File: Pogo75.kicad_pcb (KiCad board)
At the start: 2 copper layers, 57 parts, among them J2 Conn_01x05, J3 Conn_01x11, J4 Conn_01x11, J5 Conn_01x11, K1 Mod1, K2 Mod2, K3 Mod3, K4 Mod4, SW1 SW_Push, U1 W25Q128JVS, U3 XC6206PxxxMR-Regulator_Linear, Y1 Crystal_GND24_Small

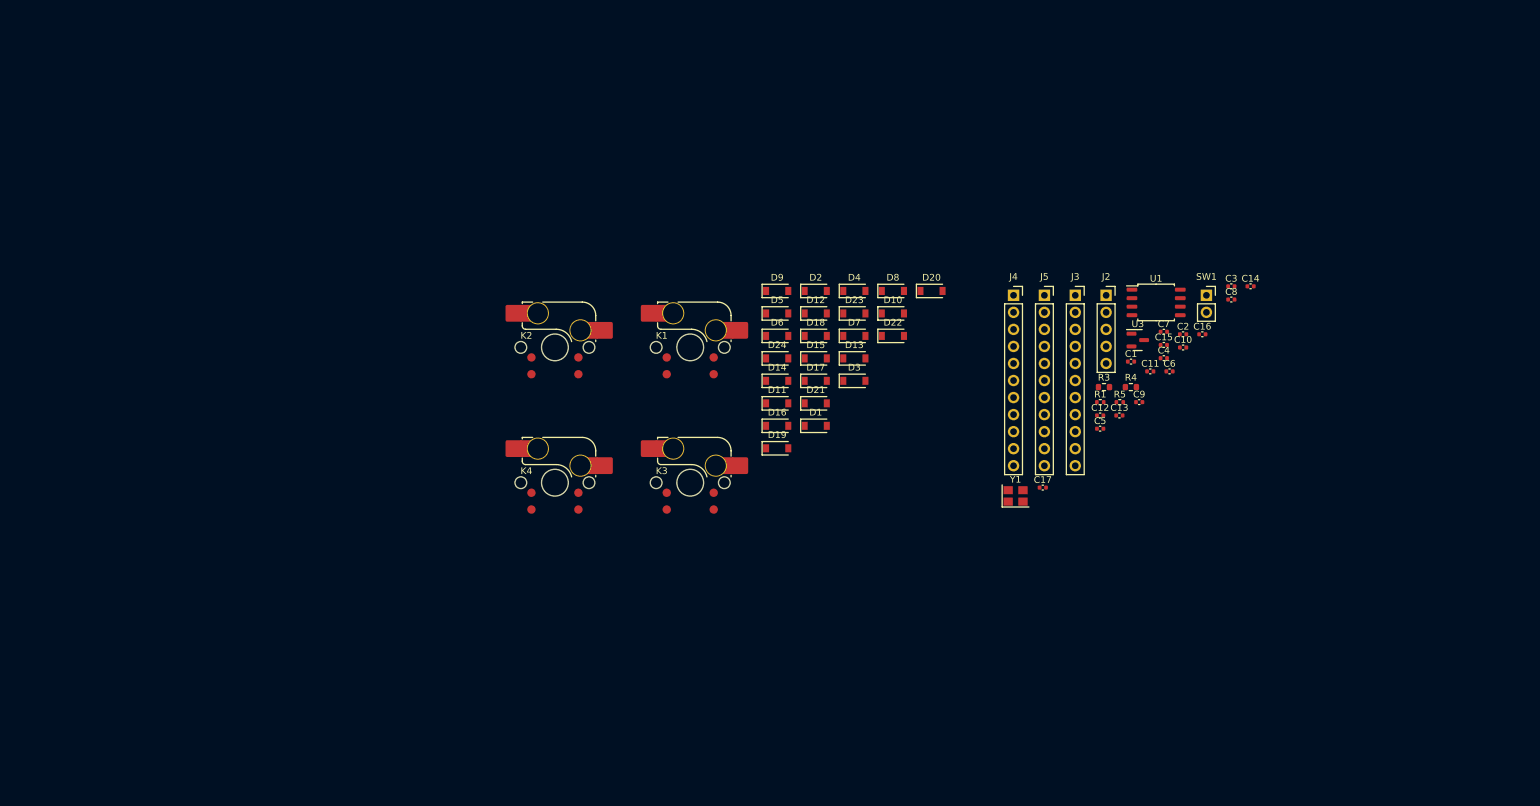
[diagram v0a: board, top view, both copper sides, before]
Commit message: Assigned footprints
Macropad + RP2040
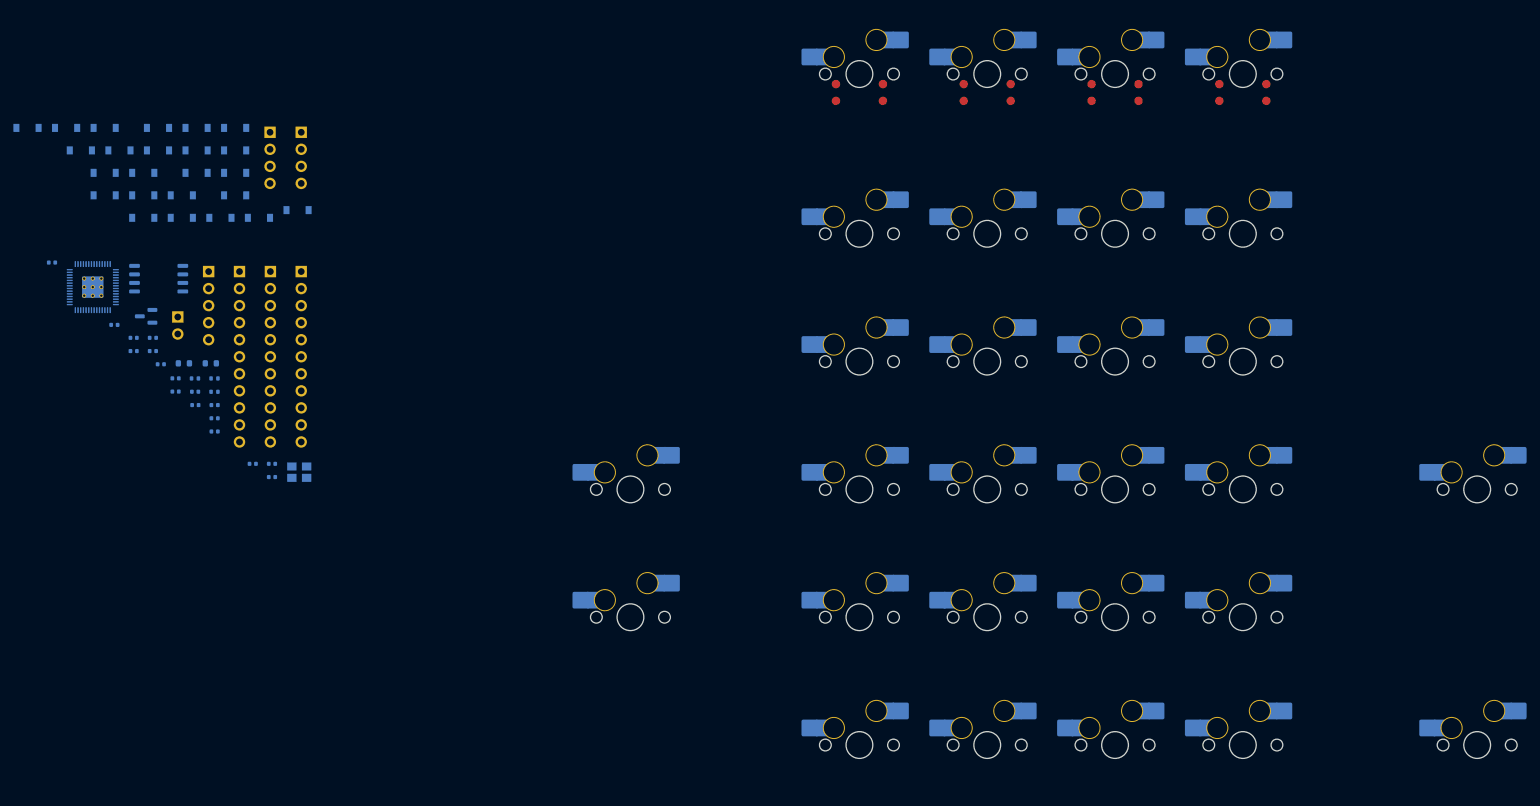
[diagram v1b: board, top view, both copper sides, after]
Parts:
- added F1: OLED1, Connector_PinHeader_2.54mm:PinHeader_1x04_P2.54mm_Vertical, B.Cu at (70.1, 49.2)
- added F2: OLED2, Connector_PinHeader_2.54mm:PinHeader_1x04_P2.54mm_Vertical, B.Cu at (74.8, 49.2)
- added K10: 8, marbastlib-mx:SW_MX_HS_1u, B.Cu at (177.0, 83.3)
- added K11: 9, marbastlib-mx:SW_MX_HS_1u, B.Cu at (196.1, 83.3)
- added K12: SW_Push, marbastlib-mx:SW_MX_HS_1u, B.Cu at (215.1, 83.3)
- added K13: 4, marbastlib-mx:SW_MX_HS_1u, B.Cu at (158.0, 102.4)
- added K14: 5, marbastlib-mx:SW_MX_HS_1u, B.Cu at (177.0, 102.4)
- added K15: 6, marbastlib-mx:SW_MX_HS_1u, B.Cu at (196.1, 102.4)
- added K16: SW_Push, marbastlib-mx:SW_MX_HS_1u, B.Cu at (215.1, 102.4)
- added K17: 1, marbastlib-mx:SW_MX_HS_1u, B.Cu at (158.0, 121.4)
- added K18: 2, marbastlib-mx:SW_MX_HS_1u, B.Cu at (177.0, 121.4)
- added K19: 3, marbastlib-mx:SW_MX_HS_1u, B.Cu at (196.1, 121.4)
- added K20: SW_Push, marbastlib-mx:SW_MX_HS_1u, B.Cu at (215.1, 121.4)
- added K21: 0, marbastlib-mx:SW_MX_HS_1u, B.Cu at (158.0, 140.5)
- added K22: ., marbastlib-mx:SW_MX_HS_1u, B.Cu at (177.0, 140.5)
- added K23: SW_Push, marbastlib-mx:SW_MX_HS_1u, B.Cu at (196.1, 140.5)
- added K24: Enter, marbastlib-mx:SW_MX_HS_1u, B.Cu at (215.1, 140.5)
- added K5: Num, marbastlib-mx:SW_MX_HS_1u, B.Cu at (158.0, 64.3)
- added K6: /, marbastlib-mx:SW_MX_HS_1u, B.Cu at (177.0, 64.3)
- added K7: *, marbastlib-mx:SW_MX_HS_1u, B.Cu at (196.1, 64.3)
- added K8: -, marbastlib-mx:SW_MX_HS_1u, B.Cu at (215.1, 64.3)
- added K9: 7, marbastlib-mx:SW_MX_HS_1u, B.Cu at (158.0, 83.3)
- added KO-1: 4, marbastlib-mx:SW_MX_HS_1u, B.Cu at (123.8, 102.4)
- added KO-2: 4, marbastlib-mx:SW_MX_HS_1u, B.Cu at (250.0, 102.4)
- added KO-3: 4, marbastlib-mx:SW_MX_HS_1u, B.Cu at (123.8, 121.4)
- added KO-4: 4, marbastlib-mx:SW_MX_HS_1u, B.Cu at (250.0, 140.5)
- added R2: R_Small, Resistor_SMD:R_0402_1005Metric, B.Cu at (61.8, 85.9)
- added U2: RP2040, Sleep-footprints:RP2040-QFN-56, B.Cu at (43.7, 72.2)
- C1, C10, C11, C12, C13, C14, C15, C16, C17, C2, C3, C4, C5, C6, C7, C8, C9, D1, D10, D11, D12, D13, D14, D15, D16, D17, D18, D19, D2, D20, D21, D22, D23, D24, D3, D4, D5, D6, D7, D8, D9, J2, J3, J4, J5, K1, K2, K3, K4, R1, R3, R4, R5, SW1, U1, U3, Y1: moved to B.Cu
- moved C14 178.7 mm to (37.6, 68.6), turned to 180 degrees
- moved C10 159.3 mm to (46.9, 77.9), turned to 180 degrees
- moved C16 155.3 mm to (53.8, 83.7), turned to 180 degrees
- moved C8 155.2 mm to (59.0, 89.8), turned to 180 degrees
- moved C15 153.6 mm to (49.8, 79.8), turned to 180 degrees
- moved SW1 153.4 mm to (56.4, 76.7), turned to 180 degrees
- moved C3 152.6 mm to (61.8, 89.8), turned to 180 degrees
- moved C4 150.7 mm to (52.6, 81.8), turned to 180 degrees
- moved U1 148.7 mm to (53.5, 71.0), turned to 180 degrees
- moved C6 148.2 mm to (56.0, 87.8), turned to 180 degrees
- moved U3 147.9 mm to (51.6, 76.6), turned to 180 degrees
- moved C2 144.9 mm to (61.8, 91.8), turned to 180 degrees
- moved C5 144.5 mm to (49.8, 81.8), turned to 180 degrees
- moved C12 141.7 mm to (52.6, 79.8), turned to 180 degrees
- moved R4 141.2 mm to (57.3, 83.6), turned to 180 degrees
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
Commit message: Modified enc footprint
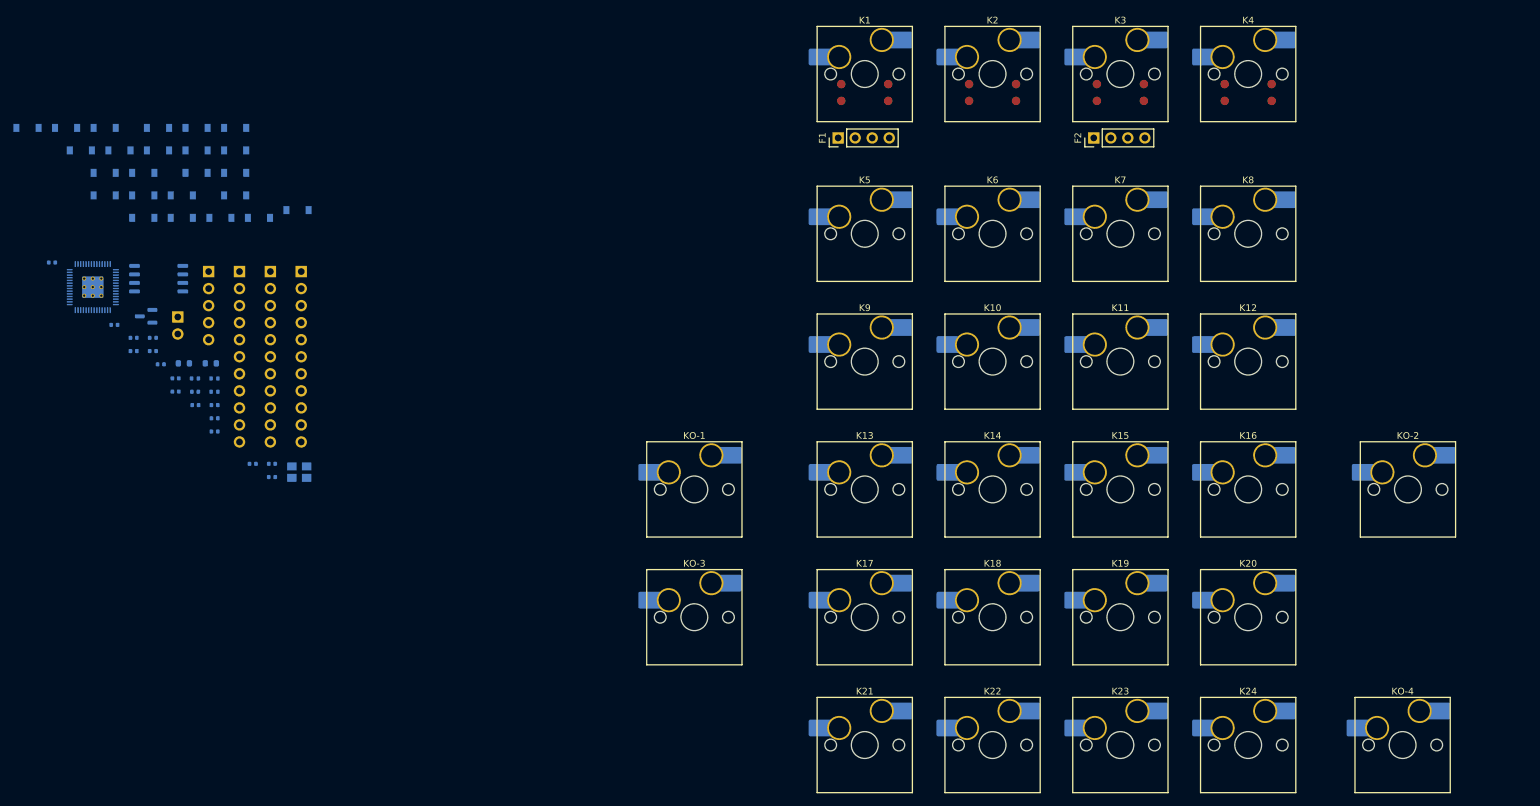
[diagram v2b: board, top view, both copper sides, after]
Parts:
- F1, F2: moved to F.Cu
- K1, K2, K3, K4: footprint marbastlib-mx:SW_MX_HS_1u_Enc -> Switch_Keyboard_Hotswap_Kailh:SW_Hotswap_Kailh_MX_plated_1.00u_Enc; moved to F.Cu
- K10, K11, K12, K13, K14, K15, K16, K17, K18, K19, K20, K21, K22, K23, K24, K5, K6, K7, K8, K9, KO-1, KO-2, KO-3, KO-4: footprint marbastlib-mx:SW_MX_HS_1u -> Switch_Keyboard_Hotswap_Kailh:SW_Hotswap_Kailh_MX_plated_1.00u; moved to F.Cu
- moved F2 118.1 mm to (192.9, 50.0), turned to 90 degrees
- moved F1 84.7 mm to (154.8, 50.0), turned to 90 degrees
- moved KO-4 11.1 mm to (238.9, 140.5), turned to 0 degrees
- moved KO-2 10.3 mm to (239.7, 102.4), turned to 0 degrees
- moved KO-1 9.52 mm to (133.3, 102.4), turned to 0 degrees
- moved KO-3 9.52 mm to (133.3, 121.4), turned to 0 degrees
- moved K10 0.79 mm to (177.8, 83.3), turned to 0 degrees
- moved K12 0.79 mm to (215.9, 83.3), turned to 0 degrees
- moved K14 0.79 mm to (177.8, 102.4), turned to 0 degrees
- moved K16 0.79 mm to (215.9, 102.4), turned to 0 degrees
- moved K18 0.79 mm to (177.8, 121.4), turned to 0 degrees
- moved K2 0.79 mm to (177.8, 40.5), turned to 0 degrees
- moved K20 0.79 mm to (215.9, 121.4), turned to 0 degrees
- moved K22 0.79 mm to (177.8, 140.5), turned to 0 degrees
- moved K24 0.79 mm to (215.9, 140.5), turned to 0 degrees
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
